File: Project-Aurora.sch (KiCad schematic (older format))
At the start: 52 parts, among them P1 USB_OTG, P2 FLASH_HDR, SW1 Reset, U1 IS31FL3732, U2 Freescale_K20P64M72SF1, U3 TPS62086, U5 IS31FL3732, U6 Case-Ground, X1 CRYSTAL_SMD

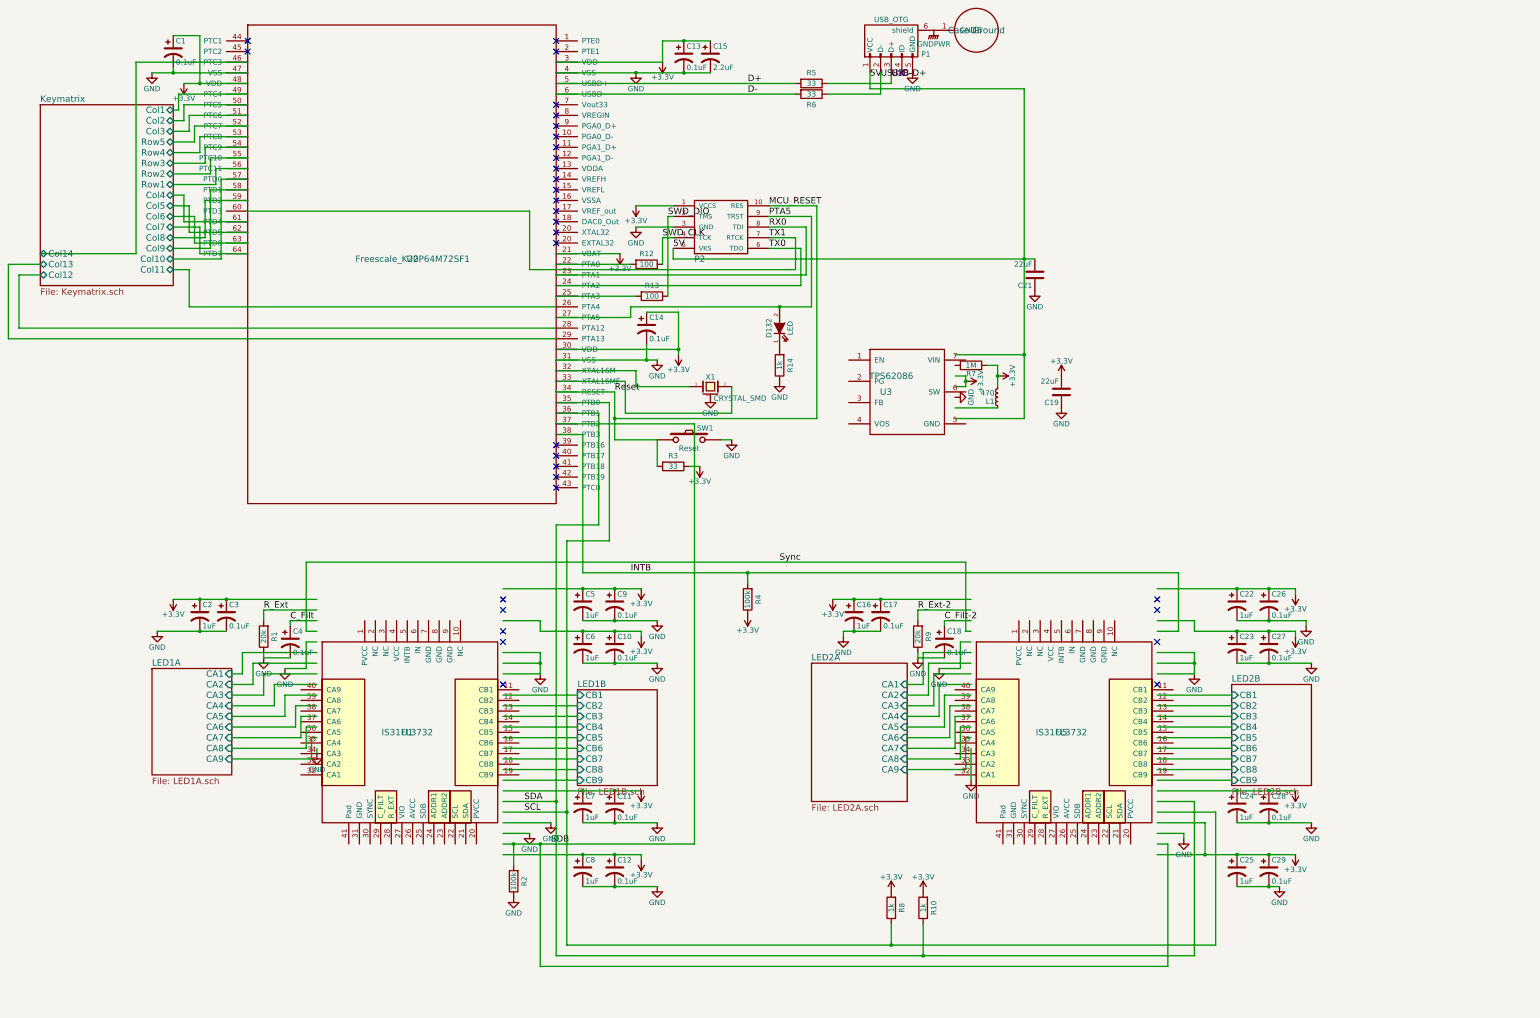
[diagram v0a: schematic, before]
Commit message: Added Fiducials, i2c Testpoints and a Filter-Cap
Fiducials: 4 Two-Sided feducials in the Corners, 4 Feducials on the Back near the ICs (these might be Overkill)
i2c Testpoints: Makes debugging less of a hassle, also tuned track-lengths of SCL and SDA
Filter-Cap: Supposed to prevent high-pitched buzzing during load
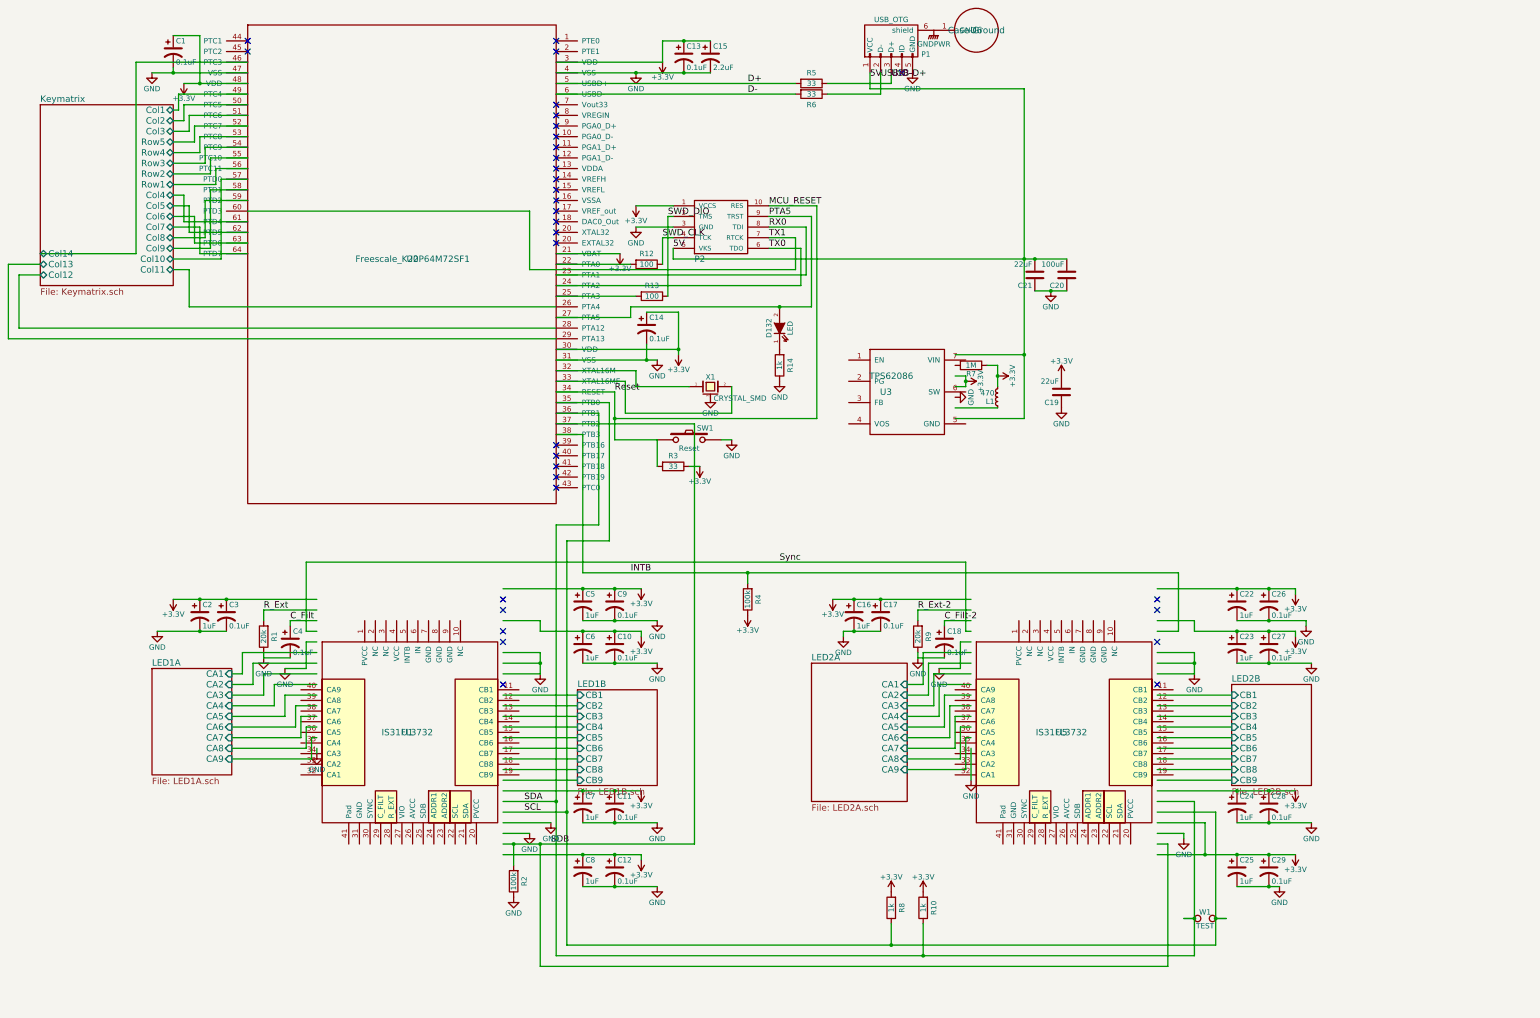
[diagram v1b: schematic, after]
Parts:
- added C20: 100uF, Capacitors_SMD:C_0805, symbol C
- added W1: TEST, Connect:PINHEAD1-2, symbol TEST
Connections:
- wire segments 304 -> 307

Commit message: Forgot some Stuff in the last Commit
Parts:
- removed U2: Freescale_K20P64M72SF1, Housings_QFP:LQFP-64_10x10mm_Pitch0.5mm, symbol Freescale_K20P64M72SF1
- removed U5: IS31FL3732, Housings_DFN_QFN:UQFN-40-1EP_5x5mm_Pitch0.4mm, symbol IS31FL3732
- added U2: MK20DX256VLH7, Housings_QFP:LQFP-64_10x10mm_Pitch0.5mm, symbol MK20DX256VLH7
- added U4: IS31FL3732, Housings_DFN_QFN:UQFN-40-1EP_5x5mm_Pitch0.4mm, symbol IS31FL3732
- P2: footprint mx2a:JLINK_NEEDLE -> Keyboard_Stuff:JLINK_NEEDLE
- SW1: footprint mx2a:KSEM31GLFS -> Keyboard_Stuff:KSEM31GLFS
- U3: footprint mx2a:VSON-7 -> Keyboard_Stuff:VSON-7
- U6: footprint mx2a:PKRHC -> Keyboard_Stuff:PKRHC
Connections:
- net labels added: PTA12, PTA13, PTA4, PTC3
- net labels removed: Reset, USB-D+, USB-D-
- wire segments 307 -> 216
- no-connect marks 33 -> 34
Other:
- moved on the sheet: C1, C10, C11, C12, C13, C14, C15, C16, C17, C18, C19, C2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

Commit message: Picked more appropriate i2c Debug Port
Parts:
- W1: footprint Connect:PINHEAD1-2 -> Measurement_Points:Test_Point_2Pads
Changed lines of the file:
@@
 F 0 "W1" H 11200 6310 50  0000 C CNN
 F 1 "TEST" H 11200 6180 50  0000 C CNN
-F 2 "Connect:PINHEAD1-2" H 11200 6250 50  0001 C CNN
+F 2 "Measurement_Points:Test_Point_2Pads" H 11200 6250 50  0001 C CNN
 F 3 "" H 11200 6250 50  0000 C CNN
 	1    11200 6250

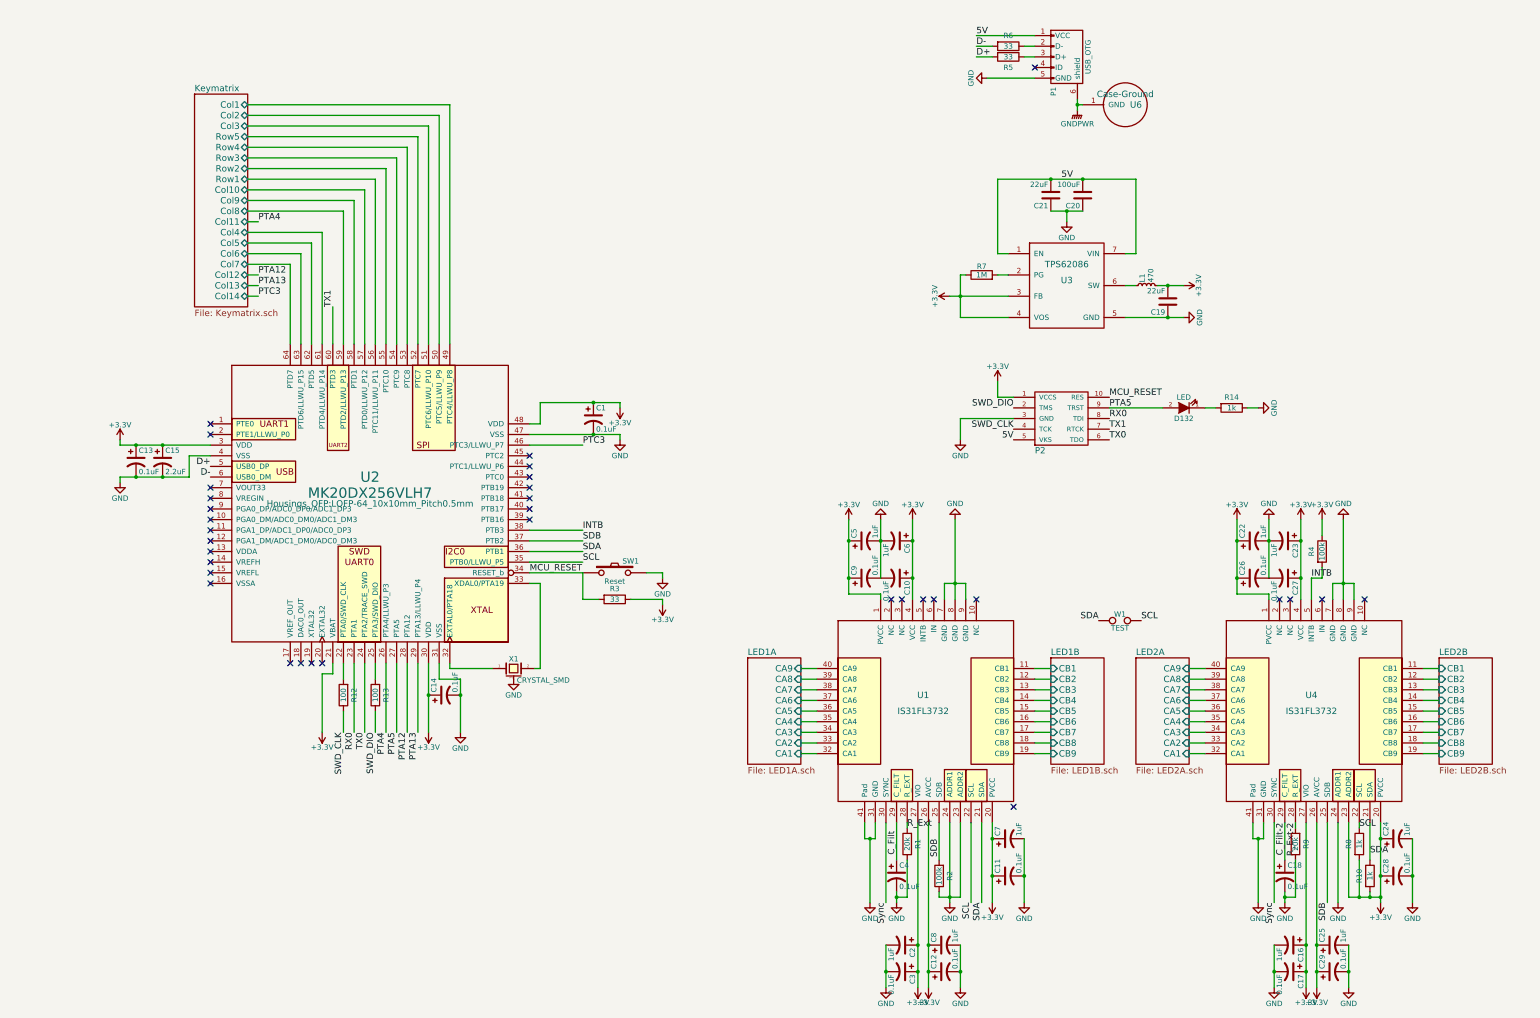
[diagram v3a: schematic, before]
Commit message: Switched from using a Dedicated one to the MCUs integrated Voltage Regulator for 3.3V. The LED-Drivers are now using 5V.
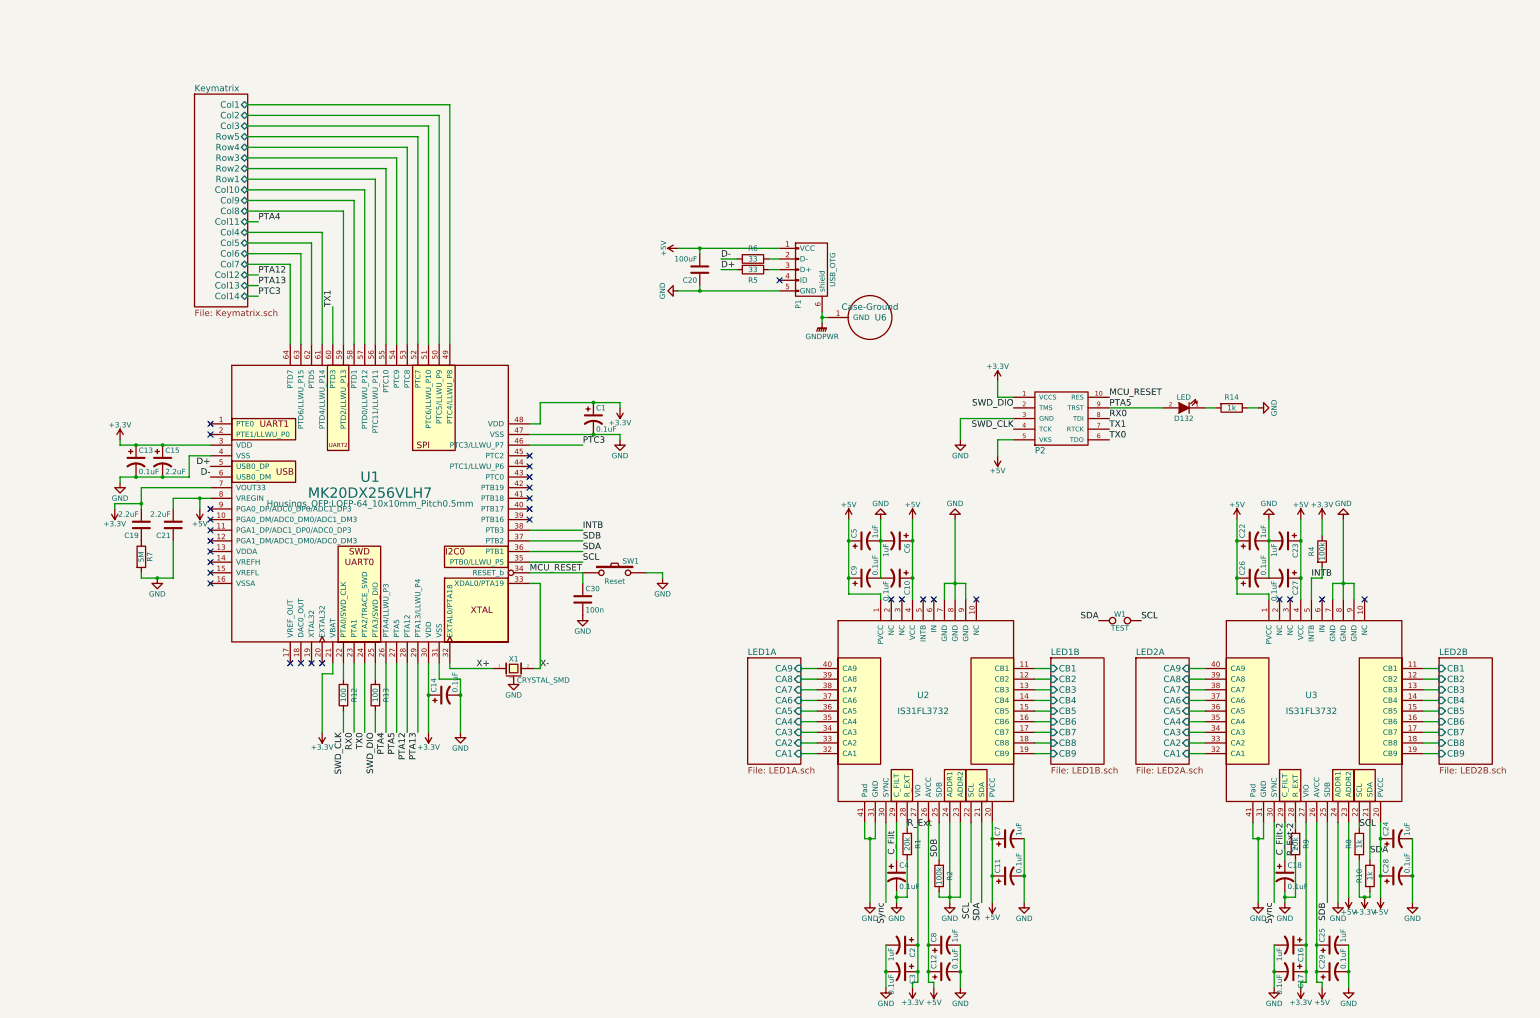
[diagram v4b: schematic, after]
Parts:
- removed L1: 470, Inductors_NEOSID:Neosid_Inductor_SM-NE29_SMD1008, symbol L_Small
- removed R3: 33, Resistors_SMD:R_0805, symbol R
- removed U3: TPS62086, Keyboard_Stuff:VSON-7, symbol TPS62086
- added C30: 100n, Capacitors_SMD:C_0805, symbol C
- C19, C21: value 22uF -> 2.2uF
- R7: value 1M -> 5M
- renumbered U2 to U1, U1 to U2, U4 to U3
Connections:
- net 5V is gone; now on net +5V: C20.2, C21.2, P1.1 (VCC), P2.5 (VKS)
- net +3V3: now also U1.7 (VOUT33); no longer C10.1, C11.1, C12.1, C22.1, C23.1, C24.1, C25.1, C26.1, C27.1, C28.1, C29.1, C5.1, C6.1, C7.1, C8.1, C9.1, R7.1, U2.1 (PVCC), U2.20 (PVCC), U2.26 (AVCC), U2.4 (VCC), U3.1 (PVCC), U3.20 (PVCC), U3.23 (ADDR2), U3.26 (AVCC), U3.4 (VCC)
- net GND: now also R7.2, C30.2; no longer C19.1
- net MCU_RESET: now also C30.1
- net X+: now reaches U1.32 (EXTAL0/PTA18), X1.1
- net X-: now reaches U1.33 (XDAL0/PTA19), X1.2
- net +5V: now reaches U1.8 (VREGIN)
- net +5V: now also C10.1, C11.1, C12.1, C22.1, C23.1, C24.1, C25.1, C26.1, C27.1, C28.1, C29.1, C5.1, C6.1, C7.1, C8.1, C9.1, U2.1 (PVCC), U2.20 (PVCC), U2.26 (AVCC), U2.4 (VCC), U3.1 (PVCC), U3.20 (PVCC), U3.23 (ADDR2), U3.26 (AVCC), U3.4 (VCC)
- new net: C19.1, R7.1
- no-connect marks 34 -> 31
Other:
- moved on the sheet: C19, C20, C21, P1, R5, R6, R7, U6

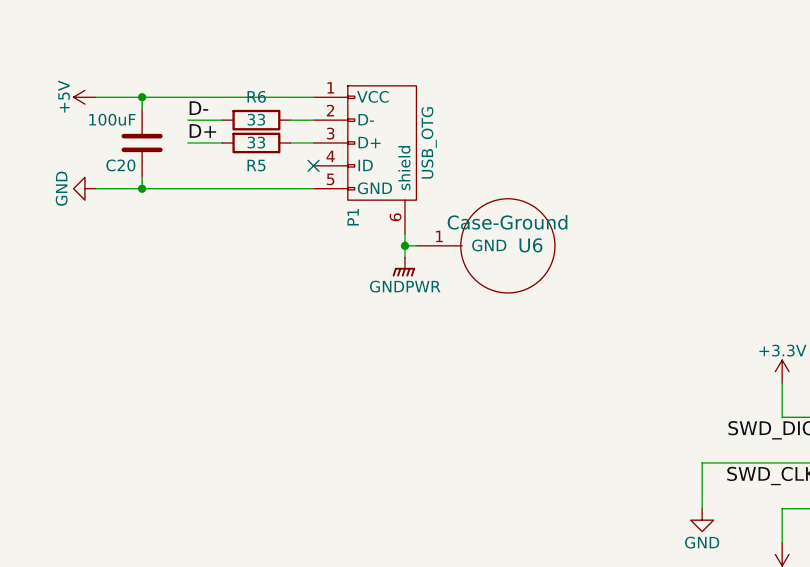
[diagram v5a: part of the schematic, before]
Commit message: Properly named Case Ground.
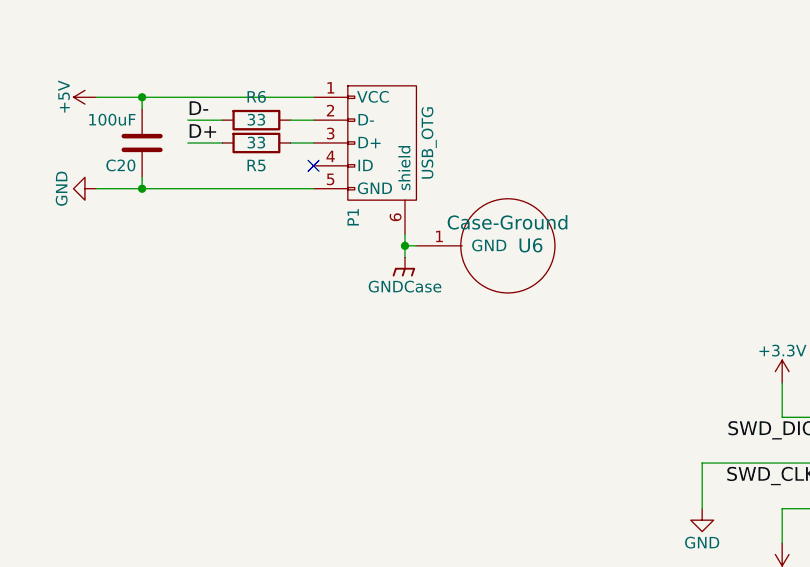
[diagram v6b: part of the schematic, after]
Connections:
- net GNDPWR renamed GNDCase
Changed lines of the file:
@@
 Text Label 12850 8150 3    60   ~ 0
 R_Ext-2
-$Comp
-L GNDPWR #PWR014
-U 1 1 56C65F67
-P 8400 3450
-F 0 "#PWR014" H 8400 3250 50  0001 C CNN
-F 1 "GNDPWR" H 8400 3320 50  0000 C CNN
-F 2 "" H 8400 3400 50  0000 C CNN
-F 3 "" H 8400 3400 50  0000 C CNN
-	1    8400 3450
-	1    0    0    -1
-$EndComp
-$Comp
-L Case-Ground U6
-U 1 1 56CA63BE
-P 8850 3400
-F 0 "U6" H 8950 3400 60  0000 C CNN
-F 1 "Case-Ground" H 8850 3500 60  0000 C CNN
-F 2 "Keyboard_Stuff:PKRHC" H 8850 3400 60  0001 C CNN
-F 3 "" H 8850 3400 60  0000 C CNN
-	1    8850 3400
-	1    0    0    -1
-$EndComp
 NoConn ~ 3400 6650
 NoConn ~ 3500 6650
@@
 	-1   0    0    1
 $EndComp
+$Comp
+L GNDCase #Case?
+U 1 1 5707D0CD
+P 8400 3450
+F 0 "#Case?" H 8400 3250 50  0001 C CNN
+F 1 "GNDCase" H 8400 3320 50  0000 C CNN
+F 2 "" H 8400 3400 50  0000 C CNN
+F 3 "" H 8400 3400 50  0000 C CNN
+	1    8400 3450
+	1    0    0    -1
+$EndComp
+$Comp
+L Case-Ground U6
+U 1 1 56CA63BE
+P 8850 3400
+F 0 "U6" H 8950 3400 60  0000 C CNN
+F 1 "Case-Ground" H 8850 3500 60  0000 C CNN
+F 2 "Keyboard_Stuff:PKRHC" H 8850 3400 60  0001 C CNN
+F 3 "" H 8850 3400 60  0000 C CNN
+	1    8850 3400
+	1    0    0    -1
+$EndComp
 $EndSCHEMATC

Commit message: Did some visual cleanup.
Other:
- moved on the sheet: D132, R14

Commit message: Added Debug-Port
In order to avoid buying the JLink Needle.
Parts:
- added P10, P11, P12, P3, P4, P5, P6, P7, P8, P9: DBG, Connect:PINTST, symbol CONN_01X01
- C30: value 100n -> 0.1uF
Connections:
- net +3V3: now also P3.1 (P1)
- net +5V: now also P7.1 (P1)
- net GND: now also P5.1 (P1)
- net MCU_RESET: now also P8.1 (P1)
- net PTA5: now also P9.1 (P1)
- net RX0: now also P10.1 (P1)
- net SWD_CLK: now also P6.1 (P1)
- net SWD_DIO: now also P4.1 (P1)
- net TX0: now also P12.1 (P1)
- net TX1: now also P11.1 (P1)
